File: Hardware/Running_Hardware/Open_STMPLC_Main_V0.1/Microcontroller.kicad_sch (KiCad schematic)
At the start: 43 parts, among them SW3 Switch, U2 STM32F407ZGTx, U9 TPS3430WDRC, Y1 32.768kHz, Y2 48MHz

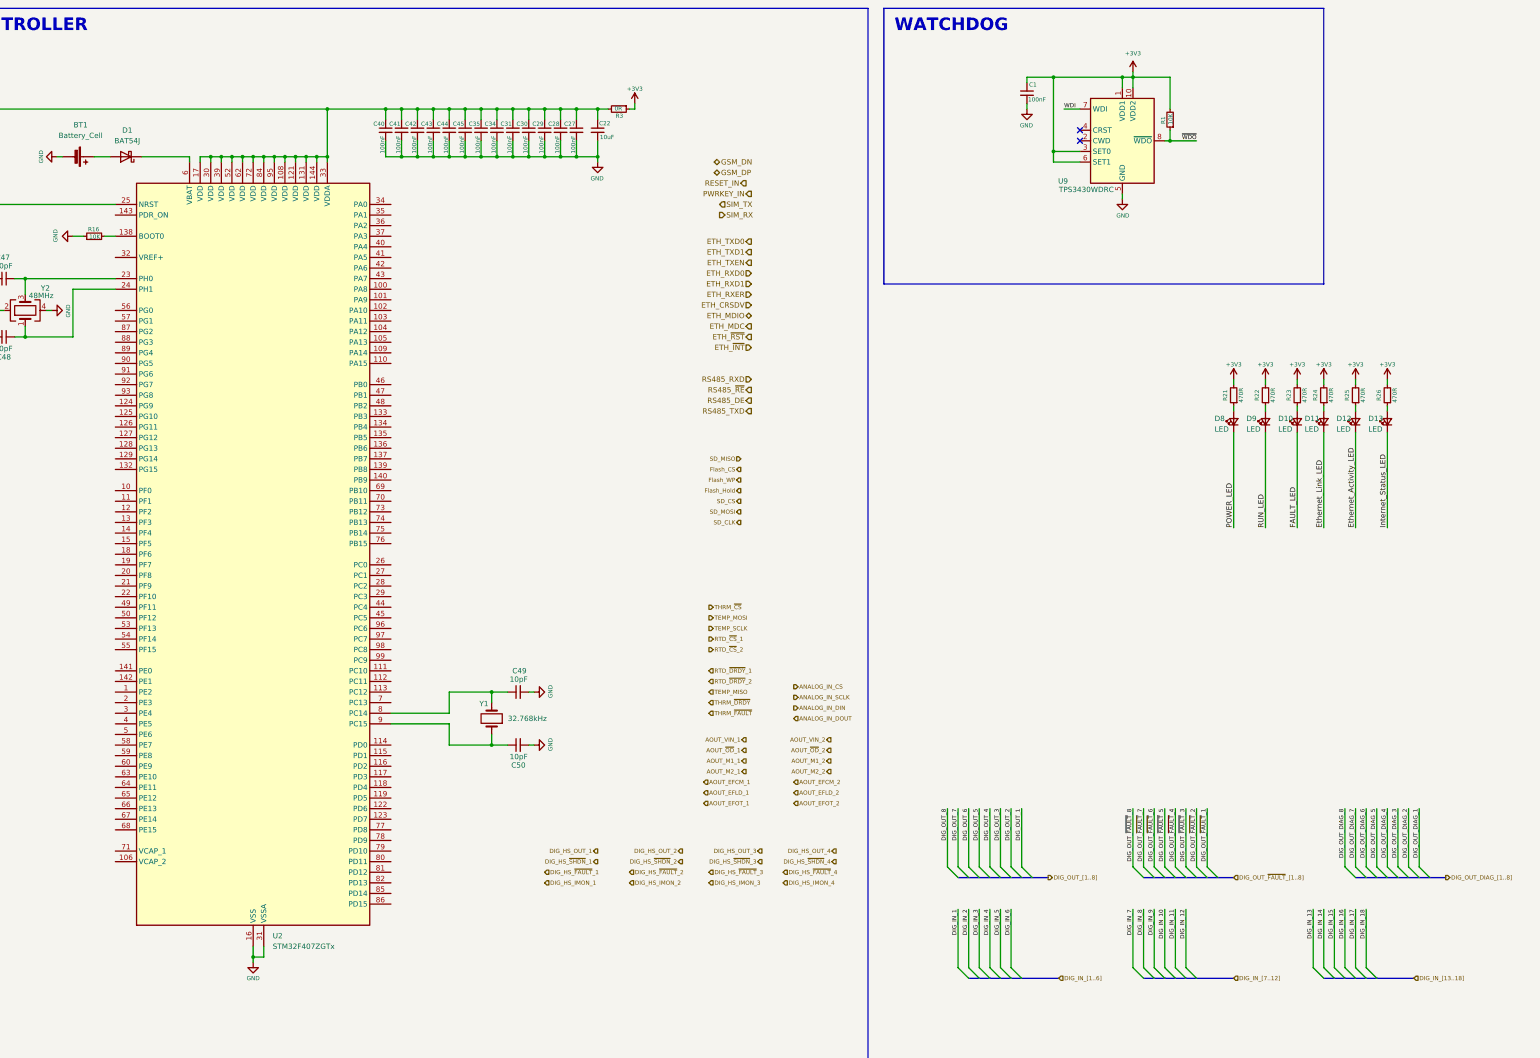
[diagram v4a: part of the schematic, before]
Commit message: Main PCB watchdog and USB add
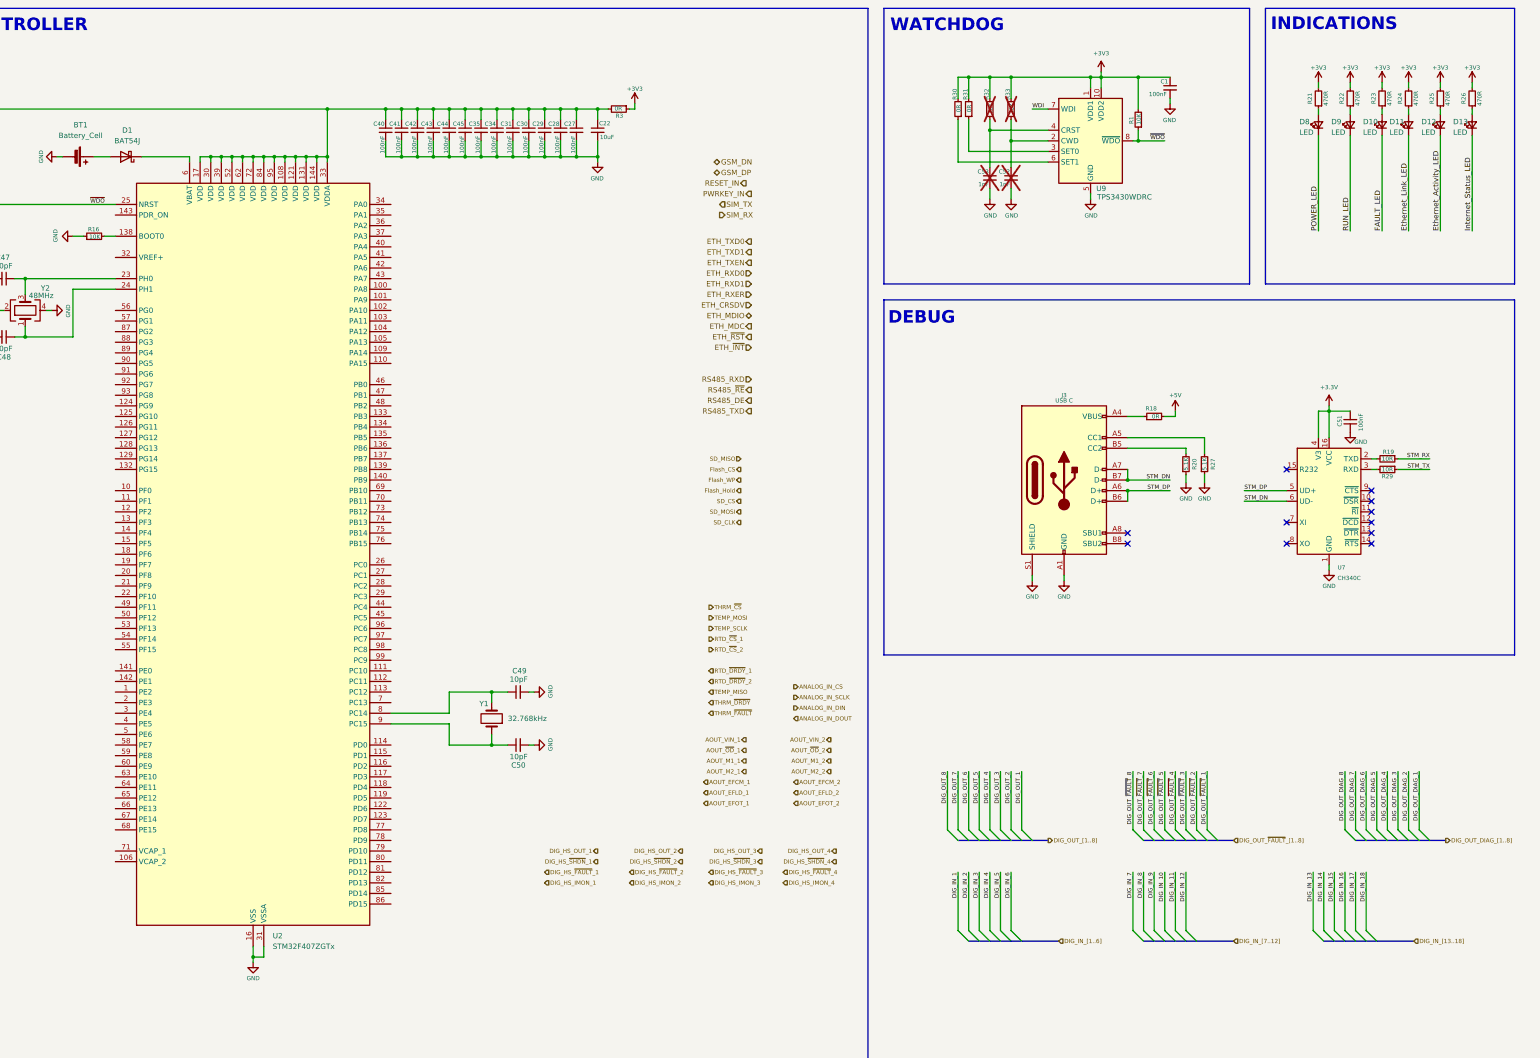
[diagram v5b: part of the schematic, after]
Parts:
- added C51: 100nF, Capacitor_SMD:C_0603_1608Metric_Pad1.08x0.95mm_HandSolder, symbol Device:C_Small
- added C52, C53: 1nF, Capacitor_SMD:C_0603_1608Metric_Pad1.08x0.95mm_HandSolder, symbol Device:C_Small
- added J3: USB C, Connector_USB:USB_C_Receptacle_GCT_USB4115-03-C, symbol Connector:USB_C_Receptacle_USB2.0
- added R18, R30, R31: 0R, Resistor_SMD:R_0603_1608Metric_Pad0.98x0.95mm_HandSolder, symbol Device:R_Small
- added R19, R29: 10R, Resistor_SMD:R_0603_1608Metric_Pad0.98x0.95mm_HandSolder, symbol jlcpcb-basic-resistor-0805:4.7k
- added R20, R27: 5.1K, Resistor_SMD:R_0603_1608Metric_Pad0.98x0.95mm_HandSolder, symbol jlcpcb-basic-resistor-0805:4.7k
- added R32, R33: 10K, Resistor_SMD:R_0603_1608Metric_Pad0.98x0.95mm_HandSolder, symbol Device:R_Small
- added U7: CH340C, Package_SO:SOIC-16_3.9x9.9mm_P1.27mm, symbol Interface_USB:CH340G
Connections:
- net +3V3: now also R30.2, R31.2, R32.2, R33.2; no longer U9.3 (SET0), U9.6 (SET1)
- net GND: now also C51.1, C52.2, C53.2, J3.A1 (GND), J3.A12 (GND), J3.B1 (GND), J3.B12 (GND), J3.S1 (SHIELD), R20.1, R27.1, U7.1 (GND)
- net ~{WDO}: now also C46.1, R15.2, SW3.2, U2.25 (NRST)
- net at U9.2 (CWD): now also C52.1, R33.1
- net at U9.4 (CRST): now also C53.1, R32.1
- new net: R30.1, U9.6 (SET1)
- new net: J3.A4 (VBUS), J3.A9 (VBUS), J3.B4 (VBUS), J3.B9 (VBUS), R18.1
- new net: R31.1, U9.3 (SET0)
- new net: R29.2, U7.3 (RXD)
- new net: R19.2, U7.2 (TXD)
- new net: J3.B5 (CC2), R20.2
- new net: J3.A5 (CC1), R27.2
- new net +3.3V: C51.2, U7.16 (VCC), U7.4 (V3)
- new net +5V: R18.2
- new net STM_DN: J3.A7 (D-), J3.B7 (D-), U7.6 (UD-)
- new net STM_DP: J3.A6 (D+), J3.B6 (D+), U7.5 (UD+)
- new net STM_RX: R19.1
- new net STM_TX: R29.1
- no-connect marks 2 -> 11
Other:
- note added: "DEBUG"
- note added: "INDICATIONS"
- moved on the sheet: C1, D10, D11, D12, D13, D8, D9, R1, R21, R22, R23, R24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

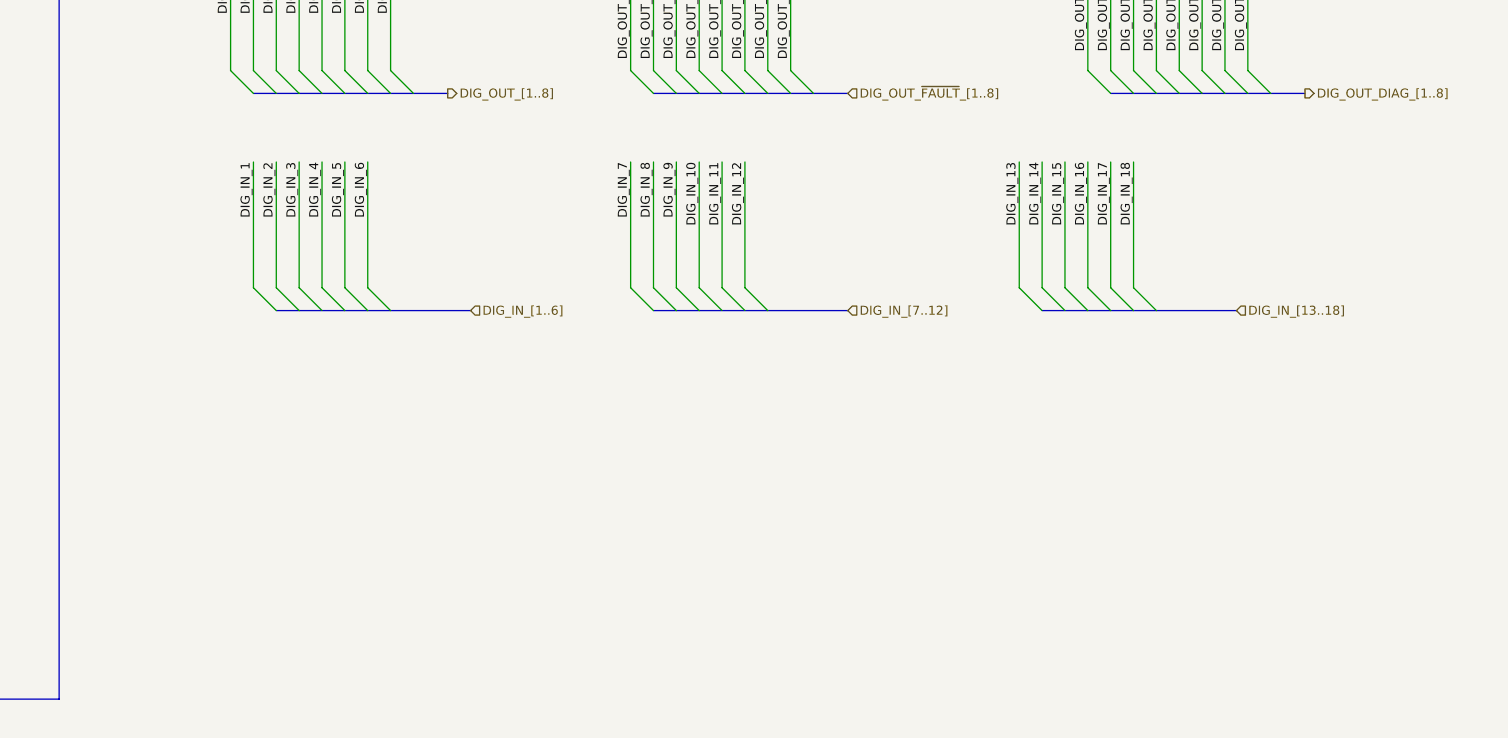
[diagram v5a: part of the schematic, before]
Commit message: Input circuit added
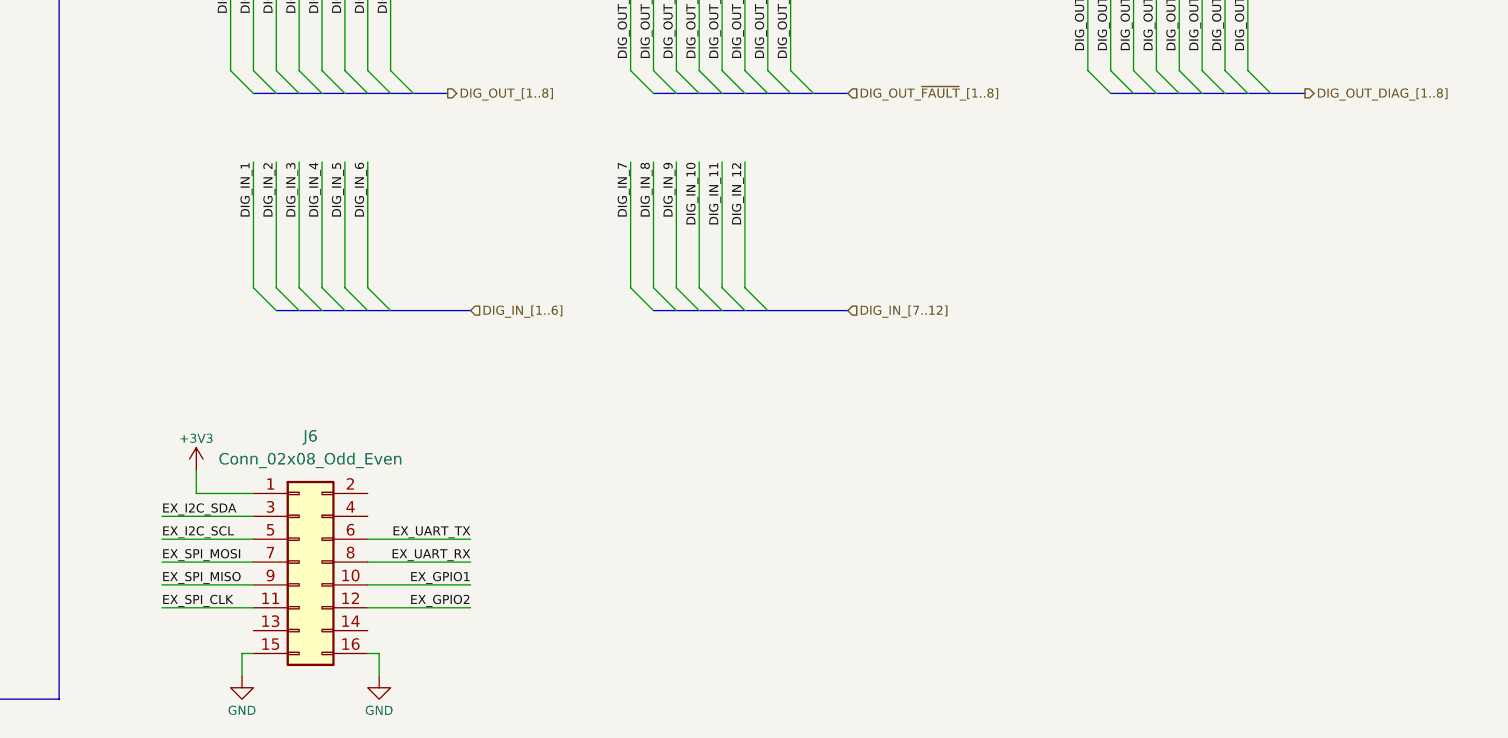
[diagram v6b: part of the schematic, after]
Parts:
- added J6: Conn_02x08_Odd_Even, symbol Connector_Generic:Conn_02x08_Odd_Even
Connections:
- net +3V3: now also J6.1 (Pin_1)
- net GND: now also J6.15 (Pin_15), J6.16 (Pin_16)
- new net EX_GPIO1: J6.10 (Pin_10)
- new net EX_GPIO2: J6.12 (Pin_12)
- new net EX_I2C_SCL: J6.5 (Pin_5)
- new net EX_I2C_SDA: J6.3 (Pin_3)
- new net EX_SPI_CLK: J6.11 (Pin_11)
- new net EX_SPI_MISO: J6.9 (Pin_9)
- new net EX_SPI_MOSI: J6.7 (Pin_7)
- new net EX_UART_RX: J6.8 (Pin_8)
- new net EX_UART_TX: J6.6 (Pin_6)

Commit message: Pin mapping IO connector
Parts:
- removed D10, D11, D12, D13, D8, D9: LED, LED_SMD:LED_0603_1608Metric_Pad1.05x0.95mm_HandSolder, symbol Device:LED_Small
- removed R21, R22, R23, R24, R25, R26: 470R, Resistor_SMD:R_0603_1608Metric_Pad0.98x0.95mm_HandSolder, symbol Device:R_Small
- BT1: footprint (none) -> Battery:BatteryHolder_MYOUNG_BS-07-A1BJ001_CR2032
- J1: renamed from J6; footprint (none) -> Connector_PinSocket_2.54mm:PinSocket_2x08_P2.54mm_Horizontal
- J2: renamed from J3; footprint Connector_USB:USB_C_Receptacle_GCT_USB4115-03-C -> Connector_USB:USB_C_Receptacle_GCT_USB4105-xx-A_16P_TopMnt_Horizontal
- renumbered C46 to C1, C42 to C10, C43 to C11, C44 to C12, C45 to C13, C35 to C14, C34 to C16, C31 to C18, C49 to C19, C47 to C2, C50 to C20, C30 to C21, C29 to C23, C28 to C24, C27 to C26, C22 to C27, C53 to C28, C52 to C29, C48 to C3, C1 to C30, C51 to C31, C40 to C8, C41 to C9, R15 to R1, R20 to R10, R27 to R11, R19 to R12, R29 to R13, R16 to R2, R30 to R4, R31 to R5, R32 to R6, R33 to R7, R1 to R8, R18 to R9, SW3 to SW1, U2 to U1, U9 to U3, U7 to U4, Y2 to Y1, Y1 to Y2
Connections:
- net +3.3V is gone; now on net +3V3: C31.2, U4.16 (VCC), U4.4 (V3)
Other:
- note removed: "INDICATIONS"

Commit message: IO board layout
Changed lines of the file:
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@@
+		)
+	)
+	(label "WDI"
+		(at 213.36 49.53 0)
+		(effects
+			(font
+				(size 1 1)
+			)
+			(justify left bottom)
 		)
 	)
